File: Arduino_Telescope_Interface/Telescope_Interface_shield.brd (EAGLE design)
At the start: 53.3 x 80 mm, 30 parts, among them IC1 40106N, IC2 24LC256P, J1 RJ45, J11 455-1750-1-ND, J12 455-1750-1-ND, J4 455-1750-1-ND, J8 455-1750-1-ND, J9 455-1750-1-ND, SW2 MOMENTARY-SWITCH-SPST-PTH-6.0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

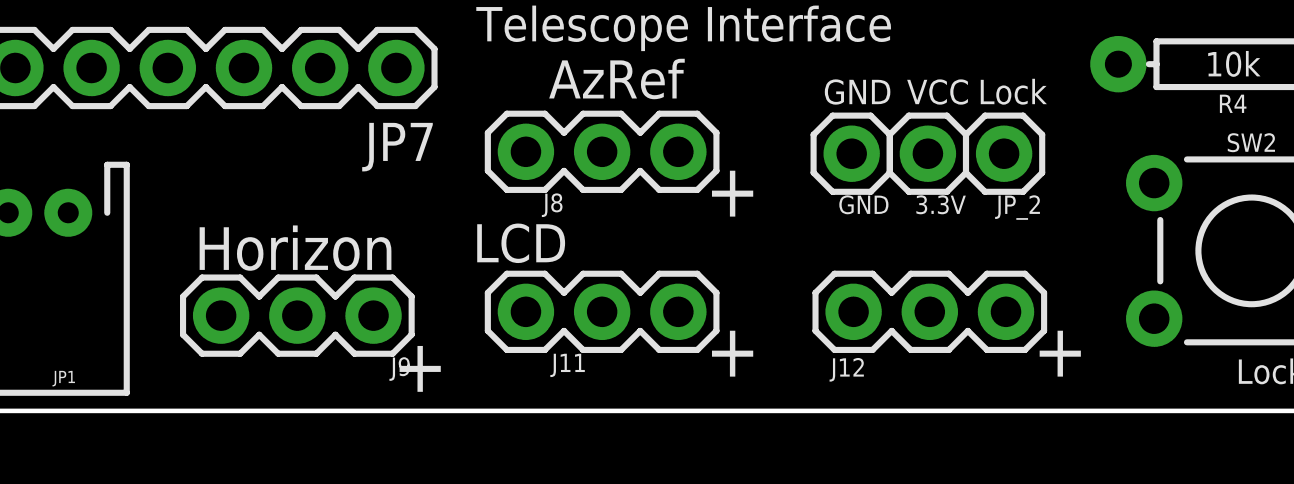
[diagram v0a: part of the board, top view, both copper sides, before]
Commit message: latest  changes in design, etc
Update design to separate out power monitoring.  Lots of other stuff too.
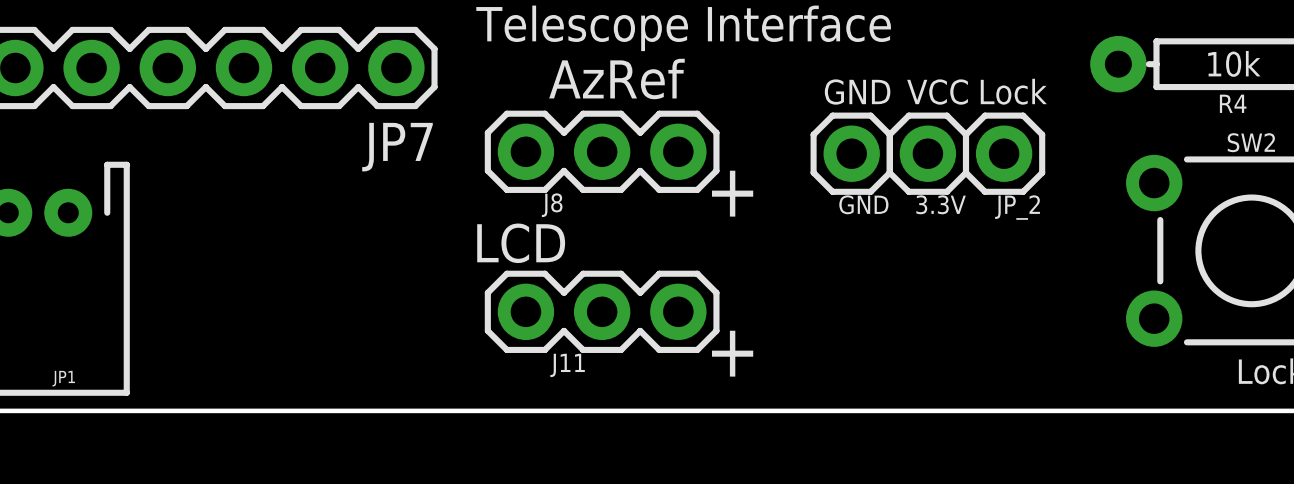
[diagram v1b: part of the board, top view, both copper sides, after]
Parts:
- removed J12, J9: 455-1750-1-ND, SparkFun-Connectors:1X03
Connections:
- net 5V: no longer J12.1, J9.1
- net GND: no longer J12.2, J9.2
- net HORIZON: no longer J9.3
- net ZENITH: no longer J12.3
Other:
- board text removed: "Horizon"
